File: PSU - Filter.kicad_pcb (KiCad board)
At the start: 2 copper layers, 92.7 x 62.2 mm, 36 parts, among them J2 +12V, J3 GND, J4 -12V, U1 LM317, U2 LM337

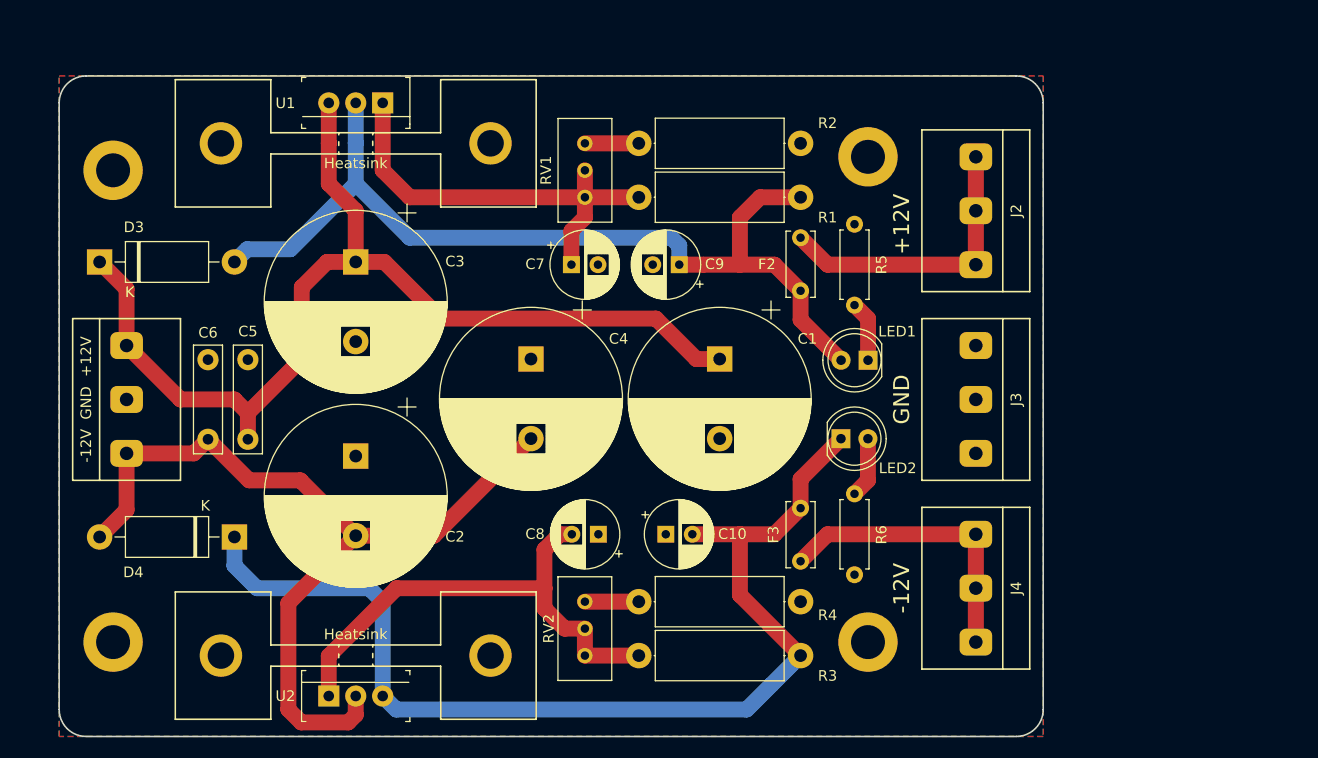
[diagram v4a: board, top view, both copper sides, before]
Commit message: Adapted for KiCad6. Also fixed an error in silkscreen for the filter
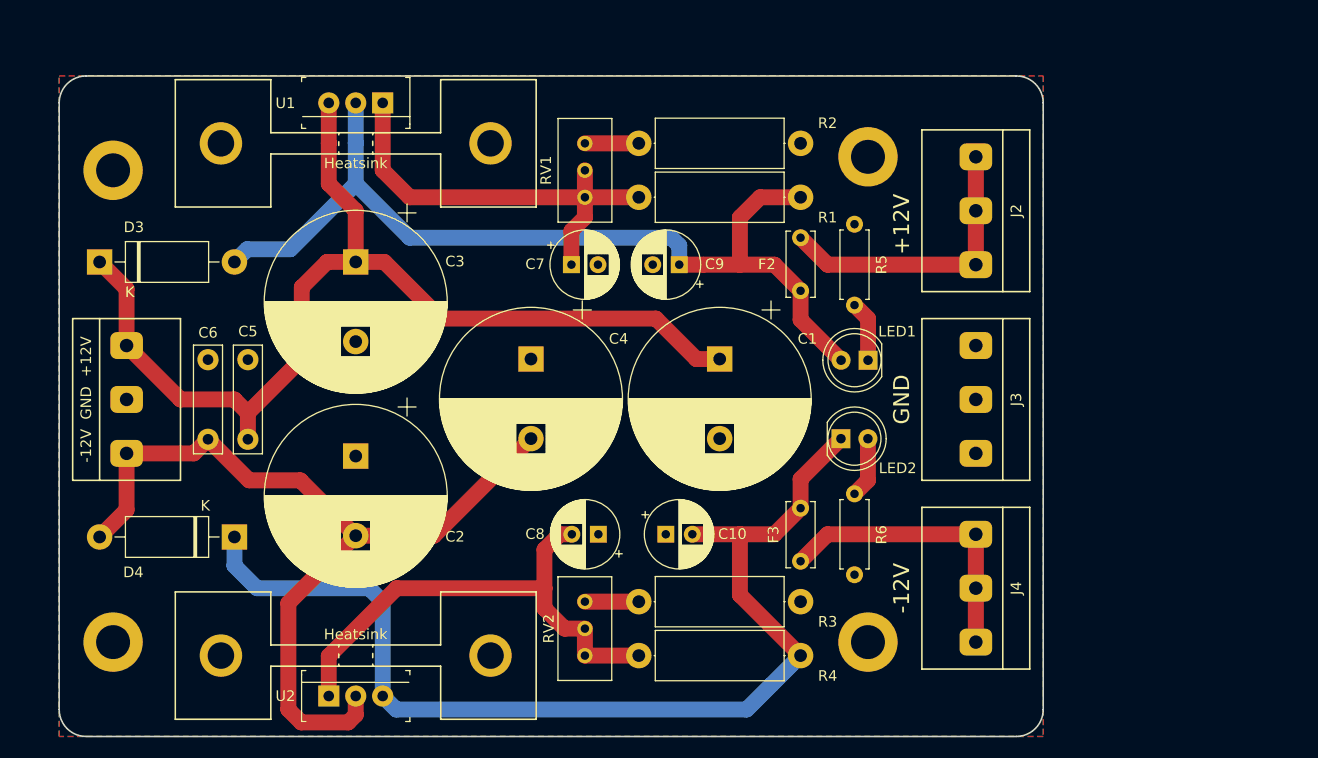
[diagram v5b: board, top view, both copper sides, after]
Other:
- net class Default removed
- board text added: "KraakenStuff PSU (filter board) v.0.4"
- board text removed: "KraakenStuff PSU (filter board) v.0.3"
